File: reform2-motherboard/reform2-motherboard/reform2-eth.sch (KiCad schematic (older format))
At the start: 7 parts

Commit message: reform2: schematic work, mainly power, display, first footprint tests
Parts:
- removed U?: KSZ9031RNXCA, Package_DFN_QFN:QFN-48-1EP_7x7mm_P0.5mm_EP5.15x5.15mm, symbol Interface_Ethernet:KSZ9031RNXCA
- C22, C23, C24, C25, C26: renamed from C?; footprint Capacitors_SMD:C_0603_HandSoldering -> Capacitor_SMD:C_0603_1608Metric
- P1: renamed from P?; footprint J0G-0003NL:PULSE_J0G-0003NL -> footprints:PULSE_J0G-0003NL
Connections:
- net labels added: ETH0_A+, ETH0_A-, ETH0_B+, ETH0_B-, ETH0_C+, ETH0_C-, ETH0_D+, ETH0_D-, ETH0_LED_LINK, ETH0_LED_RX
- net labels removed: ENET_LED_LINK, ENET_LED_RX, TRD0_N, TRD0_P, TRD1_N, TRD1_P, TRD2_N, TRD2_P, TRD3_N, TRD3_P

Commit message: WIP reform2: more schematics ground work on USB, PCIe, Display, Audio, Power
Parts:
- C22, C23, C24, C25, C26: symbol reform-motherboard-rescue:C_Small -> reform2-motherboard-rescue:C_Small-reform-motherboard-rescue
- P1: symbol reform-motherboard-rescue:J0G-0003NL -> reform2-motherboard-rescue:J0G-0003NL-reform-motherboard-rescue
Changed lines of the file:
@@
 Sheet 4 9
 Title "MNT Reform 2 Ethernet"
-Date "2019-06-14"
+Date "2019-06-21"
 Rev "0.1"
 Comp "MNT Research GmbH"
@@
 $EndDescr
 $Comp
-L reform-motherboard-rescue:J0G-0003NL P1
+L reform2-motherboard-rescue:J0G-0003NL-reform-motherboard-rescue P1
 U 1 1 5A04FC73
 P 6050 3650
+AR Path="/5A04FC73" Ref="P1"  Part="1"
+AR Path="/5D06A32E/5A04FC73" Ref="P1"  Part="1"
 F 0 "P1" H 5246 5811 50  0000 L BNN
 F 1 "J0G-0003NL" H 5247 1341 50  0000 L BNN
@@
 $EndComp
 $Comp
-L reform-motherboard-rescue:+3V3 #PWR0139
+L reform2-motherboard-rescue:+3V3-reform-motherboard-rescue #PWR0139
 U 1 1 5A04FD4C
 P 4150 4750
+AR Path="/5A04FD4C" Ref="#PWR0139"  Part="1"
+AR Path="/5D06A32E/5A04FD4C" Ref="#PWR0139"  Part="1"
 F 0 "#PWR0139" H 4150 4600 50  0001 C CNN
 F 1 "+3V3" H 4150 4890 50  0000 C CNN
@@
 $EndComp
 $Comp
-L reform-motherboard-rescue:C_Small C22
+L reform2-motherboard-rescue:C_Small-reform-motherboard-rescue C22
 U 1 1 5A04FD85
 P 3900 5000
+AR Path="/5A04FD85" Ref="C22"  Part="1"
+AR Path="/5D06A32E/5A04FD85" Ref="C22"  Part="1"
 F 0 "C22" H 3910 5070 50  0000 L CNN
 F 1 "0.1uF" H 3910 4920 50  0000 L CNN
@@
 $EndComp
 $Comp
-L reform-motherboard-rescue:GND #PWR0140
+L reform2-motherboard-rescue:GND-reform-motherboard-rescue #PWR0140
 U 1 1 5A04FDB4
 P 3900 5100
+AR Path="/5A04FDB4" Ref="#PWR0140"  Part="1"
+AR Path="/5D06A32E/5A04FDB4" Ref="#PWR0140"  Part="1"
 F 0 "#PWR0140" H 3900 4850 50  0001 C CNN
 F 1 "GND" H 3900 4950 50  0000 C CNN
@@
 $EndComp
 $Comp
-L reform-motherboard-rescue:C_Small C23
+L reform2-motherboard-rescue:C_Small-reform-motherboard-rescue C23
 U 1 1 5A05122D
 P 4350 2050
+AR Path="/5A05122D" Ref="C23"  Part="1"
+AR Path="/5D06A32E/5A05122D" Ref="C23"  Part="1"
 F 0 "C23" H 4360 2120 50  0000 L CNN
 F 1 "0.1uF" H 4360 1970 50  0000 L CNN
@@
 $EndComp
 $Comp
-L reform-motherboard-rescue:C_Small C24
+L reform2-motherboard-rescue:C_Small-reform-motherboard-rescue C24
 U 1 1 5A051336
 P 4350 2850
+AR Path="/5A051336" Ref="C24"  Part="1"
+AR Path="/5D06A32E/5A051336" Ref="C24"  Part="1"
 F 0 "C24" H 4360 2920 50  0000 L CNN
 F 1 "0.1uF" H 4360 2770 50  0000 L CNN
@@
 $EndComp
 $Comp
-L reform-motherboard-rescue:C_Small C25
+L reform2-motherboard-rescue:C_Small-reform-motherboard-rescue C25
 U 1 1 5A0513CA
 P 4350 3650
+AR Path="/5A0513CA" Ref="C25"  Part="1"
+AR Path="/5D06A32E/5A0513CA" Ref="C25"  Part="1"
 F 0 "C25" H 4360 3720 50  0000 L CNN
 F 1 "0.1uF" H 4360 3570 50  0000 L CNN
@@
 $EndComp
 $Comp
-L reform-motherboard-rescue:C_Small C26
+L reform2-motherboard-rescue:C_Small-reform-motherboard-rescue C26
 U 1 1 5A05141B
 P 4350 4450
+AR Path="/5A05141B" Ref="C26"  Part="1"
+AR Path="/5D06A32E/5A05141B" Ref="C26"  Part="1"
 F 0 "C26" H 4360 4520 50  0000 L CNN
 F 1 "0.1uF" H 4360 4370 50  0000 L CNN
@@
 $EndComp
 $Comp
-L reform-motherboard-rescue:GND #PWR0141
+L reform2-motherboard-rescue:GND-reform-motherboard-rescue #PWR0141
 U 1 1 5A118EA5
 P 4350 2150
+AR Path="/5A118EA5" Ref="#PWR0141"  Part="1"
+AR Path="/5D06A32E/5A118EA5" Ref="#PWR0141"  Part="1"
 F 0 "#PWR0141" H 4350 1900 50  0001 C CNN
 F 1 "GND" H 4350 2000 50  0000 C CNN
@@
 $EndComp
 $Comp
-L reform-motherboard-rescue:GND #PWR0142
+L reform2-motherboard-rescue:GND-reform-motherboard-rescue #PWR0142
 U 1 1 5A118FBC
 P 4350 2950
+AR Path="/5A118FBC" Ref="#PWR0142"  Part="1"
+AR Path="/5D06A32E/5A118FBC" Ref="#PWR0142"  Part="1"
 F 0 "#PWR0142" H 4350 2700 50  0001 C CNN
 F 1 "GND" H 4350 2800 50  0000 C CNN
@@
 $EndComp
 $Comp
-L reform-motherboard-rescue:GND #PWR0143
+L reform2-motherboard-rescue:GND-reform-motherboard-rescue #PWR0143
 U 1 1 5A119060
 P 4350 3750
+AR Path="/5A119060" Ref="#PWR0143"  Part="1"
+AR Path="/5D06A32E/5A119060" Ref="#PWR0143"  Part="1"
 F 0 "#PWR0143" H 4350 3500 50  0001 C CNN
 F 1 "GND" H 4350 3600 50  0000 C CNN
@@
 $EndComp
 $Comp
-L reform-motherboard-rescue:GND #PWR0144
+L reform2-motherboard-rescue:GND-reform-motherboard-rescue #PWR0144
 U 1 1 5A119104
 P 4350 4550
+AR Path="/5A119104" Ref="#PWR0144"  Part="1"
+AR Path="/5D06A32E/5A119104" Ref="#PWR0144"  Part="1"
 F 0 "#PWR0144" H 4350 4300 50  0001 C CNN
 F 1 "GND" H 4350 4400 50  0000 C CNN
@@
 $EndComp
 $Comp
-L reform-motherboard-rescue:GND #PWR0145
+L reform2-motherboard-rescue:GND-reform-motherboard-rescue #PWR0145
 U 1 1 5A119D9C
 P 7150 5550
+AR Path="/5A119D9C" Ref="#PWR0145"  Part="1"
+AR Path="/5D06A32E/5A119D9C" Ref="#PWR0145"  Part="1"
 F 0 "#PWR0145" H 7150 5300 50  0001 C CNN
 F 1 "GND" H 7150 5400 50  0000 C CNN

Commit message: WIP: reform2 motherboard: more schematics tuning, preliminary selection of most components
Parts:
- C22, C23, C24, C25, C26: Manufacturer (none) -> TDK; Manufacturer_No (none) -> CGA3E2X8R1E104K080AE
- P1: Manufacturer (none) -> Pulse; Manufacturer_No (none) -> J0G-0003NL
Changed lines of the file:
@@
 F 7 "J0G-0003NL" H 6050 3650 50  0001 L BNN "MP"
 F 8 "None" H 6050 3650 50  0001 L BNN "Package"
+F 9 "Pulse" H 6050 3650 50  0001 C CNN "Manufacturer"
+F 10 "J0G-0003NL" H 6050 3650 50  0001 C CNN "Manufacturer_No"
 	1    6050 3650
 	1    0    0    -1
@@
 F 2 "Capacitor_SMD:C_0603_1608Metric" H 3900 5000 50  0001 C CNN
 F 3 "" H 3900 5000 50  0001 C CNN
+F 4 "TDK" H 3900 5000 50  0001 C CNN "Manufacturer"
+F 5 "CGA3E2X8R1E104K080AE" H 3900 5000 50  0001 C CNN "Manufacturer_No"
 	1    3900 5000
 	1    0    0    -1
@@
 F 2 "Capacitor_SMD:C_0603_1608Metric" H 4350 2050 50  0001 C CNN
 F 3 "" H 4350 2050 50  0001 C CNN
+F 4 "TDK" H 4350 2050 50  0001 C CNN "Manufacturer"
+F 5 "CGA3E2X8R1E104K080AE" H 4350 2050 50  0001 C CNN "Manufacturer_No"
 	1    4350 2050
 	1    0    0    -1
@@
 F 2 "Capacitor_SMD:C_0603_1608Metric" H 4350 2850 50  0001 C CNN
 F 3 "" H 4350 2850 50  0001 C CNN
+F 4 "TDK" H 4350 2850 50  0001 C CNN "Manufacturer"
+F 5 "CGA3E2X8R1E104K080AE" H 4350 2850 50  0001 C CNN "Manufacturer_No"
 	1    4350 2850
 	1    0    0    -1
@@
 F 2 "Capacitor_SMD:C_0603_1608Metric" H 4350 3650 50  0001 C CNN
 F 3 "" H 4350 3650 50  0001 C CNN
+F 4 "TDK" H 4350 3650 50  0001 C CNN "Manufacturer"
+F 5 "CGA3E2X8R1E104K080AE" H 4350 3650 50  0001 C CNN "Manufacturer_No"
 	1    4350 3650
 	1    0    0    -1
@@
 F 2 "Capacitor_SMD:C_0603_1608Metric" H 4350 4450 50  0001 C CNN
 F 3 "" H 4350 4450 50  0001 C CNN
+F 4 "TDK" H 4350 4450 50  0001 C CNN "Manufacturer"
+F 5 "CGA3E2X8R1E104K080AE" H 4350 4450 50  0001 C CNN "Manufacturer_No"
 	1    4350 4450
 	1    0    0    -1

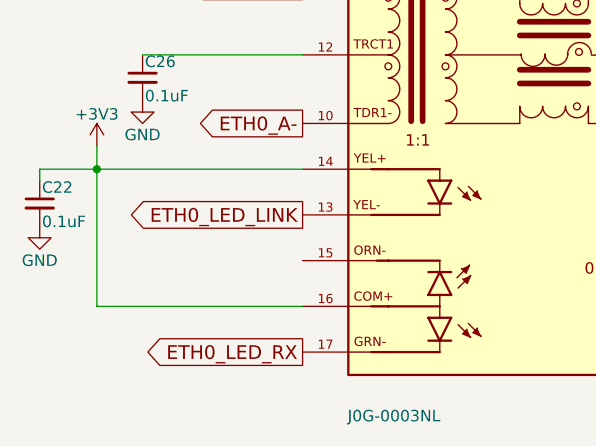
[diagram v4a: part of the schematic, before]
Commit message: WIP: reform 2 motherboard: tweaks for CL-SOM
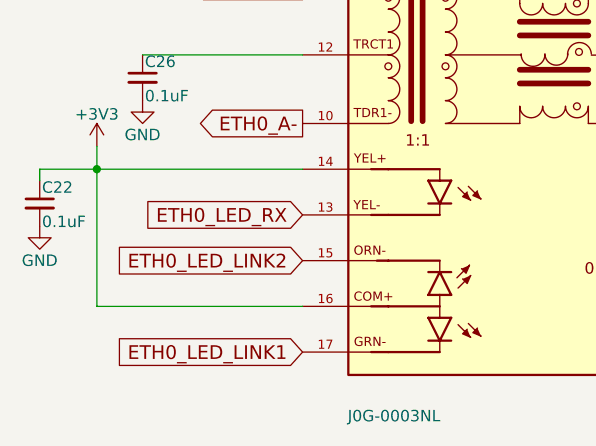
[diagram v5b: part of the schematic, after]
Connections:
- net ETH0_LED_LINK is gone; now on net ETH0_LED_RX: P1.13 (YEL-)
- net ETH0_LED_RX: no longer P1.17 (GRN-)
- net ETH0_LED_LINK2: now reaches P1.15 (ORN-)
- new net ETH0_LED_LINK1: P1.17 (GRN-)
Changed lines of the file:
@@
 Sheet 4 9
 Title "MNT Reform 2 Ethernet"
-Date "2019-07-03"
-Rev "0.1"
+Date "2019-07-09"
+Rev "0.1.1"
 Comp "MNT Research GmbH"
 Comment1 "https://mntre.com"
@@
 Wire Wire Line
 	4150 4850 4150 5450
-Text GLabel 5050 5050 0    60   Output ~ 0
-ETH0_LED_LINK
-Text GLabel 5050 5650 0    60   Output ~ 0
+Text GLabel 5050 5650 0    60   Input ~ 0
+ETH0_LED_LINK1
+Text GLabel 5050 5050 0    60   Input ~ 0
 ETH0_LED_RX
 Text GLabel 5050 2250 0    60   Output ~ 0
@@
 Text GLabel 5050 4050 0    60   Output ~ 0
 ETH0_A+
+Text GLabel 5050 5250 0    60   Input ~ 0
+ETH0_LED_LINK2
 $EndSCHEMATC

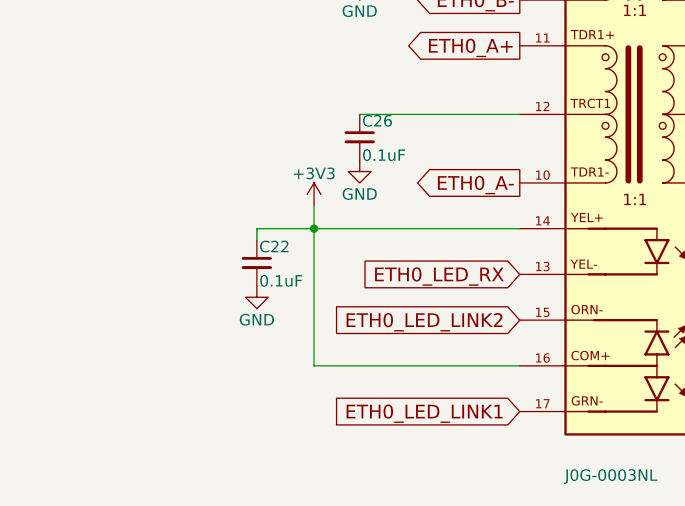
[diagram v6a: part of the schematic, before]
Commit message: reform2: motherboard final tweaks before first order
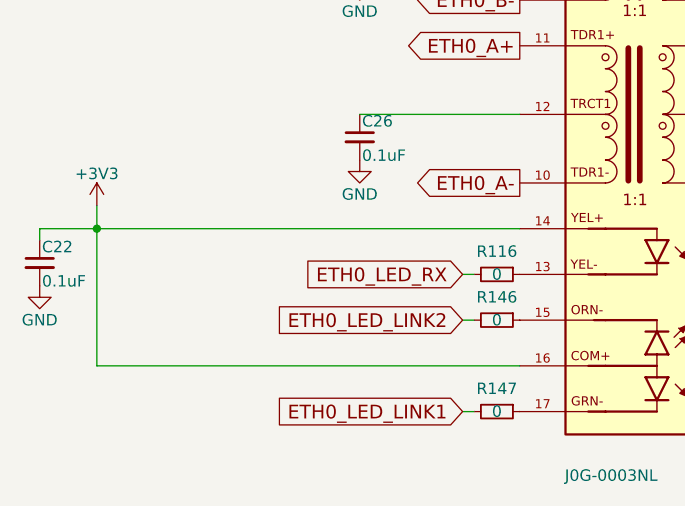
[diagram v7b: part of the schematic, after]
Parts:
- added R116, R146, R147: 0, Resistor_SMD:R_0603_1608Metric, symbol Device:R_Small
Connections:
- net ETH0_LED_LINK1: now also R147.2; no longer P1.17 (GRN-)
- net ETH0_LED_LINK2: now also R146.2; no longer P1.15 (ORN-)
- net ETH0_LED_RX: now also R116.2; no longer P1.13 (YEL-)
- new net: P1.13 (YEL-), R116.1
- new net: P1.15 (ORN-), R146.1
- new net: P1.17 (GRN-), R147.1
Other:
- moved on the sheet: C22

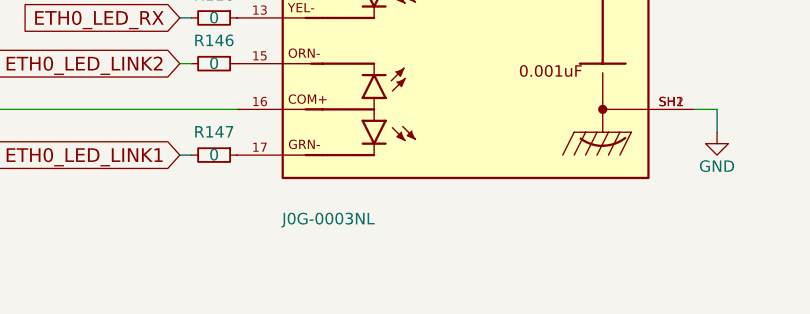
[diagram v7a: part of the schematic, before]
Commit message: reform2 motherboard: add part numbers
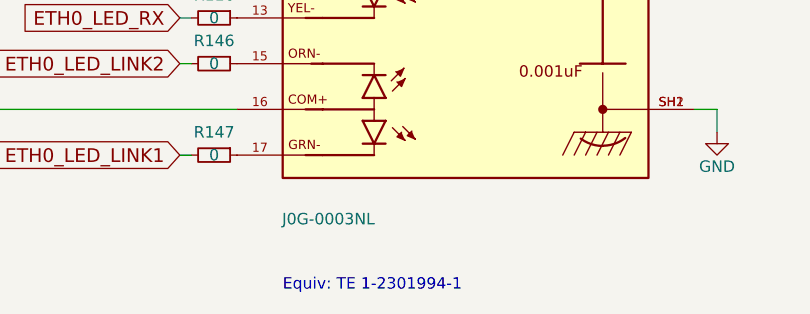
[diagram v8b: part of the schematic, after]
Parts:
- C22, C23, C24, C25, C26: Manufacturer TDK -> Yageo; Manufacturer_No CGA3E2X8R1E104K080AE -> CC0603JPX7R9BB104
- R116, R146, R147: Manufacturer (none) -> Vishay Dale; Manufacturer_No (none) -> CRCW06030000Z0EAC
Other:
- note added: "Equiv: TE 1-2301994-1"
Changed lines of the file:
@@
 F 2 "Capacitor_SMD:C_0603_1608Metric" H 4350 2050 50  0001 C CNN
 F 3 "" H 4350 2050 50  0001 C CNN
-F 4 "TDK" H 4350 2050 50  0001 C CNN "Manufacturer"
-F 5 "CGA3E2X8R1E104K080AE" H 4350 2050 50  0001 C CNN "Manufacturer_No"
+F 4 "Yageo" H 4350 2050 50  0001 C CNN "Manufacturer"
+F 5 "CC0603JPX7R9BB104" H 4350 2050 50  0001 C CNN "Manufacturer_No"
 	1    4350 2050
 	1    0    0    -1
@@
 F 2 "Capacitor_SMD:C_0603_1608Metric" H 4350 2850 50  0001 C CNN
 F 3 "" H 4350 2850 50  0001 C CNN
-F 4 "TDK" H 4350 2850 50  0001 C CNN "Manufacturer"
-F 5 "CGA3E2X8R1E104K080AE" H 4350 2850 50  0001 C CNN "Manufacturer_No"
+F 4 "Yageo" H 4350 2850 50  0001 C CNN "Manufacturer"
+F 5 "CC0603JPX7R9BB104" H 4350 2850 50  0001 C CNN "Manufacturer_No"
 	1    4350 2850
 	1    0    0    -1
@@
 F 2 "Capacitor_SMD:C_0603_1608Metric" H 4350 3650 50  0001 C CNN
 F 3 "" H 4350 3650 50  0001 C CNN
-F 4 "TDK" H 4350 3650 50  0001 C CNN "Manufacturer"
-F 5 "CGA3E2X8R1E104K080AE" H 4350 3650 50  0001 C CNN "Manufacturer_No"
+F 4 "Yageo" H 4350 3650 50  0001 C CNN "Manufacturer"
+F 5 "CC0603JPX7R9BB104" H 4350 3650 50  0001 C CNN "Manufacturer_No"
 	1    4350 3650
 	1    0    0    -1
@@
 F 2 "Capacitor_SMD:C_0603_1608Metric" H 2950 5000 50  0001 C CNN
 F 3 "" H 2950 5000 50  0001 C CNN
-F 4 "TDK" H 2950 5000 50  0001 C CNN "Manufacturer"
-F 5 "CGA3E2X8R1E104K080AE" H 2950 5000 50  0001 C CNN "Manufacturer_No"
+F 4 "Yageo" H 2950 5000 50  0001 C CNN "Manufacturer"
+F 5 "CC0603JPX7R9BB104" H 2950 5000 50  0001 C CNN "Manufacturer_No"
 	1    2950 5000
 	1    0    0    -1
@@
 F 2 "Capacitor_SMD:C_0603_1608Metric" H 4350 4450 50  0001 C CNN
 F 3 "" H 4350 4450 50  0001 C CNN
-F 4 "TDK" H 4350 4450 50  0001 C CNN "Manufacturer"
-F 5 "CGA3E2X8R1E104K080AE" H 4350 4450 50  0001 C CNN "Manufacturer_No"
+F 4 "Yageo" H 4350 4450 50  0001 C CNN "Manufacturer"
+F 5 "CC0603JPX7R9BB104" H 4350 4450 50  0001 C CNN "Manufacturer_No"
 	1    4350 4450
 	1    0    0    -1
@@
 F 2 "Resistor_SMD:R_0603_1608Metric" H 4950 5050 50  0001 C CNN
 F 3 "~" H 4950 5050 50  0001 C CNN
+F 4 "Vishay Dale" H 4950 5050 50  0001 C CNN "Manufacturer"
+F 5 "CRCW06030000Z0EAC" H 4950 5050 50  0001 C CNN "Manufacturer_No"
 	1    4950 5050
 	0    1    1    0
@@
 F 2 "Resistor_SMD:R_0603_1608Metric" H 4950 5250 50  0001 C CNN
 F 3 "~" H 4950 5250 50  0001 C CNN
+F 4 "Vishay Dale" H 4950 5250 50  0001 C CNN "Manufacturer"
+F 5 "CRCW06030000Z0EAC" H 4950 5250 50  0001 C CNN "Manufacturer_No"
 	1    4950 5250
 	0    1    1    0
@@
 F 2 "Resistor_SMD:R_0603_1608Metric" H 4950 5650 50  0001 C CNN
 F 3 "~" H 4950 5650 50  0001 C CNN
+F 4 "Vishay Dale" H 4950 5650 50  0001 C CNN "Manufacturer"
+F 5 "CRCW06030000Z0EAC" H 4950 5650 50  0001 C CNN "Manufacturer_No"
 	1    4950 5650
 	0    1    1    0
@@
 Wire Wire Line
 	4800 5050 4850 5050
+Text Notes 5250 6250 0    50   ~ 0
+Equiv: TE 1-2301994-1
 $EndSCHEMATC
